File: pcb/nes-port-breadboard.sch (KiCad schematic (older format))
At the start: 2 parts, among them J1 NES_Port_Male, J2 Conn_01x07

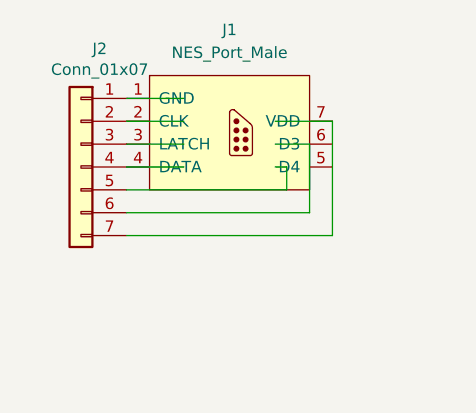
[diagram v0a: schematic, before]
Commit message: Make NES port holes bigger. Shrink board to 1.4x1.4 inches
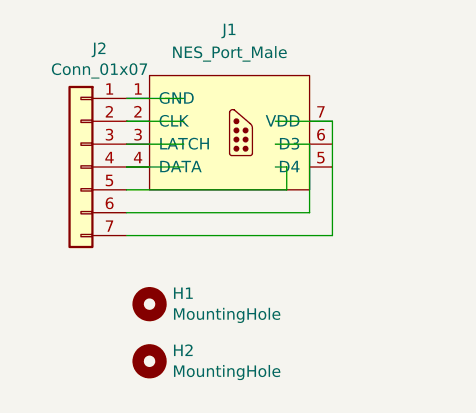
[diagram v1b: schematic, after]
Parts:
- added H1, H2: MountingHole, MountingHole:MountingHole_2.7mm_M2.5, symbol Mechanical:MountingHole
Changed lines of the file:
@@
 Sheet 1 1
 Title "NES Port Breadboard Adapter"
-Date "2021-06-09"
-Rev "1.0"
+Date "2021-07-04"
+Rev "1.0.1"
 Comp ""
 Comment1 ""
@@
 Wire Wire Line
 	5800 3700 4900 3700
+$Comp
+L Mechanical:MountingHole H1
+U 1 1 60E147EE
+P 5000 4000
+F 0 "H1" H 5100 4046 50  0000 L CNN
+F 1 "MountingHole" H 5100 3955 50  0000 L CNN
+F 2 "MountingHole:MountingHole_2.7mm_M2.5" H 5000 4000 50  0001 C CNN
+F 3 "~" H 5000 4000 50  0001 C CNN
+	1    5000 4000
+	1    0    0    -1
+$EndComp
+$Comp
+L Mechanical:MountingHole H2
+U 1 1 60E14FCE
+P 5000 4250
+F 0 "H2" H 5100 4296 50  0000 L CNN
+F 1 "MountingHole" H 5100 4205 50  0000 L CNN
+F 2 "MountingHole:MountingHole_2.7mm_M2.5" H 5000 4250 50  0001 C CNN
+F 3 "~" H 5000 4250 50  0001 C CNN
+	1    5000 4250
+	1    0    0    -1
+$EndComp
 $EndSCHEMATC

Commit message: Update schematic symbol for NES port
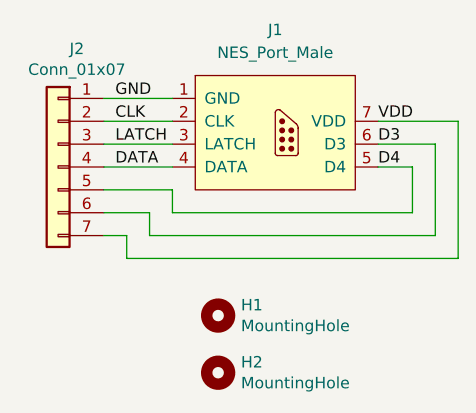
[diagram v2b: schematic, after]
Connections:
- net labels added: CLK, D3, D4, DATA, GND, LATCH, VDD
- wire segments 13 -> 19
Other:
- moved on the sheet: H1, H2, J1, J2
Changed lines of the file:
@@
 Sheet 1 1
 Title "NES Port Breadboard Adapter"
-Date "2021-07-04"
+Date "2021-07-07"
 Rev "1.0.1"
 Comp ""
@@
 $EndDescr
 $Comp
-L nes-port-breadboard:NES_Port_Male J1
-U 1 1 60C605E6
-P 5350 3250
-F 0 "J1" H 5350 3700 50  0000 C CNN
-F 1 "NES_Port_Male" H 5350 3600 50  0000 C CNN
-F 2 "nes-port-breadboard:NES_Port_Male_Horizontal" H 5350 3250 50  0001 C CNN
-F 3 "" H 5350 3250 50  0001 C CNN
-	1    5350 3250
-	1    0    0    -1
-$EndComp
-$Comp
 L Connector_Generic:Conn_01x07 J2
 U 1 1 60C61DBB
-P 4700 3400
-F 0 "J2" H 4618 3917 50  0000 C CNN
-F 1 "Conn_01x07" H 4618 3826 50  0000 C CNN
-F 2 "Connector_PinHeader_2.54mm:PinHeader_1x07_P2.54mm_Vertical" H 4700 3400 50  0001 C CNN
-F 3 "~" H 4700 3400 50  0001 C CNN
-	1    4700 3400
+P 4600 3400
+F 0 "J2" H 4518 3917 50  0000 C CNN
+F 1 "Conn_01x07" H 4518 3826 50  0000 C CNN
+F 2 "Connector_PinHeader_2.54mm:PinHeader_1x07_P2.54mm_Vertical" H 4600 3400 50  0001 C CNN
+F 3 "~" H 4600 3400 50  0001 C CNN
+	1    4600 3400
 	-1   0    0    -1
 $EndComp
-Wire Wire Line
-	5150 3100 4900 3100
-Wire Wire Line
-	5150 3200 4900 3200
-Wire Wire Line
-	5150 3300 4900 3300
-Wire Wire Line
-	5150 3400 4900 3400
-Wire Wire Line
-	5550 3400 5600 3400
-Wire Wire Line
-	5600 3400 5600 3500
-Wire Wire Line
-	5600 3500 4900 3500
-Wire Wire Line
-	5550 3300 5700 3300
-Wire Wire Line
-	5700 3300 5700 3600
-Wire Wire Line
-	5700 3600 4900 3600
-Wire Wire Line
-	5550 3200 5800 3200
-Wire Wire Line
-	5800 3200 5800 3700
-Wire Wire Line
-	5800 3700 4900 3700
 $Comp
 L Mechanical:MountingHole H1
 U 1 1 60E147EE
-P 5000 4000
-F 0 "H1" H 5100 4046 50  0000 L CNN
-F 1 "MountingHole" H 5100 3955 50  0000 L CNN
-F 2 "MountingHole:MountingHole_2.7mm_M2.5" H 5000 4000 50  0001 C CNN
-F 3 "~" H 5000 4000 50  0001 C CNN
-	1    5000 4000
+P 5300 4050
+F 0 "H1" H 5400 4096 50  0000 L CNN
+F 1 "MountingHole" H 5400 4005 50  0000 L CNN
+F 2 "MountingHole:MountingHole_2.7mm_M2.5" H 5300 4050 50  0001 C CNN
+F 3 "~" H 5300 4050 50  0001 C CNN
+	1    5300 4050
 	1    0    0    -1
 $EndComp
@@
 L Mechanical:MountingHole H2
 U 1 1 60E14FCE
-P 5000 4250
-F 0 "H2" H 5100 4296 50  0000 L CNN
-F 1 "MountingHole" H 5100 4205 50  0000 L CNN
-F 2 "MountingHole:MountingHole_2.7mm_M2.5" H 5000 4250 50  0001 C CNN
-F 3 "~" H 5000 4250 50  0001 C CNN
-	1    5000 4250
+P 5300 4300
+F 0 "H2" H 5400 4346 50  0000 L CNN
+F 1 "MountingHole" H 5400 4255 50  0000 L CNN
+F 2 "MountingHole:MountingHole_2.7mm_M2.5" H 5300 4300 50  0001 C CNN
+F 3 "~" H 5300 4300 50  0001 C CNN
+	1    5300 4300
 	1    0    0    -1
 $EndComp
+Text Label 4850 3100 0    50   ~ 0
+GND
+Wire Wire Line
+	5100 3600 5100 3500
+Wire Wire Line
+	5100 3500 4800 3500
+Wire Wire Line
+	5000 3700 5000 3600
+Wire Wire Line
+	5000 3600 4800 3600
+Wire Wire Line
+	4900 3800 4900 3700
+Wire Wire Line
+	4900 3700 4800 3700
+Text Label 4850 3400 0    50   ~ 0
+DATA
+Text Label 4850 3300 0    50   ~ 0
+LATCH
+Text Label 4850 3200 0    50   ~ 0
+CLK
+Text Label 6000 3400 0    50   ~ 0
+D4
+Text Label 6000 3300 0    50   ~ 0
+D3
+Wire Wire Line
+	6250 3300 6250 3700
+Wire Wire Line
+	6150 3400 6150 3600
+Wire Wire Line
+	5100 3400 4800 3400
+Wire Wire Line
+	5100 3300 4800 3300
+Wire Wire Line
+	5100 3200 4800 3200
+Wire Wire Line
+	5100 3100 4800 3100
+Wire Wire Line
+	6350 3200 6350 3800
+Text Label 6000 3200 0    50   ~ 0
+VDD
+$Comp
+L nes-port-breadboard:NES_Port_Male J1
+U 1 1 60C605E6
+P 5550 3250
+F 0 "J1" H 5550 3700 50  0000 C CNN
+F 1 "NES_Port_Male" H 5550 3600 50  0000 C CNN
+F 2 "nes-port-breadboard:NES_Port_Male_Horizontal" H 5550 3250 50  0001 C CNN
+F 3 "" H 5550 3250 50  0001 C CNN
+	1    5550 3250
+	1    0    0    -1
+$EndComp
+Wire Wire Line
+	6000 3400 6150 3400
+Wire Wire Line
+	6000 3200 6350 3200
+Wire Wire Line
+	6250 3300 6000 3300
+Wire Wire Line
+	5100 3600 6150 3600
+Wire Wire Line
+	5000 3700 6250 3700
+Wire Wire Line
+	4900 3800 6350 3800
 $EndSCHEMATC
